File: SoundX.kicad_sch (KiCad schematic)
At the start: 51 parts, among them CN1 EDGE_CONN, CN2 AUDIO_OUT, CN3 CONN_MIDI_IN, CN4 CONN_MIDI_OUT, U1 GAL20V8, U2 MOS_6551_ACIA, U3 YM3526, U4 6N138, U6 YM3014, U7 LM324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

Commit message: Version with MC6850 should be ready
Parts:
- removed U2: MOS_6551_ACIA, Package_DIP:DIP-28_W15.24mm_Socket_LongPads, symbol W65C51S:W65C51S
- added U2: MC6850, Package_DIP:DIP-24_W15.24mm_Socket_LongPads, symbol Interface_UART:MC6850
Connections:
- net +5V: now also U2.10 (CS1), U2.12 (VCC), U2.8 (CS0)
- net GND: now also U2.1 (VSS), U2.23 (~{DCD}), U2.24 (~{CTS})
- net a0: now also U2.11 (RS)
- net clock_acia: now also U2.3 (Rx_CLK), U2.4 (Tx_CLK)
- net d0: now also U2.22 (D0)
- net d1: now also U2.21 (D1)
- net d2: now also U2.20 (D2)
- net d3: now also U2.19 (D3)
- net d4: now also U2.18 (D4)
- net d5: now also U2.17 (D5)
- net d6: now also U2.16 (D6)
- net d7: now also U2.15 (D7)
- net phi2: now also U2.14 (E)
- net r_~{w}: now also U2.13 (R/~{W})
- net rxd_ttl: now also U2.2 (Rx_Data)
- net txd_ttl: now also U2.6 (Tx_Data)
- net ~{irq}: now also U2.7 (~{IRQ})
- net ~{midi_cs}: now also U2.9 (CS2)
- net at FB3.2: now also R2.1; no longer R2.2
- net at X2.5 (OUT): now also R2.2; no longer R2.1
- no-connect marks 20 -> 18
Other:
- note added: "ACTIVE-LOW!"
- note removed: "NOTE 3 MHZ CRYSTAL! THIS ALLOWS REACHING THE 31250 BPS REQUIRED FOR MIDI CONFIGURING THE ACIA FOR 19200 BPS (DIVISOR = 96 => 3000000/96 = 31250) WE ALSO PROVIDE PARALLEL R AND SERIES C FOR W65C51S, BUT I'D RECOMMEND USING AN OLDER 6551"
- note removed: "Pin 7 must float with external clock"
- moved on the sheet: C11, R2

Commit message: Final touches for V2
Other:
- moved on the sheet: U1

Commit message: Fixes after rebasing (???)
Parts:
- JP1, JP2, JP3, JP4, JP5, JP6: now left out of the parts list
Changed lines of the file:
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@@
 		(unit 1)
 		(exclude_from_sim no)
-		(in_bom yes)
+		(in_bom no)
 		(on_board yes)
 		(dnp no)
@@
 		(unit 1)
 		(exclude_from_sim no)
-		(in_bom yes)
+		(in_bom no)
 		(on_board yes)
 		(dnp no)
@@
 		(unit 1)
 		(exclude_from_sim no)
-		(in_bom yes)
+		(in_bom no)
 		(on_board yes)
 		(dnp no)
@@
 		(unit 1)
 		(exclude_from_sim no)
-		(in_bom yes)
+		(in_bom no)
 		(on_board yes)
 		(dnp no)
@@
 		(unit 1)
 		(exclude_from_sim no)
-		(in_bom yes)
+		(in_bom no)
 		(on_board yes)
 		(dnp no)
@@
 		(unit 1)
 		(exclude_from_sim no)
-		(in_bom yes)
+		(in_bom no)
 		(on_board yes)
 		(dnp no)

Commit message: Readd some P/Ns and add 5mm-pitch footprint for DIN-5 connector
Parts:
- C1, C15: MouserPN (none) -> 710-860010472002
- C13: MouserPN 810-FG28C0G1H471JNT6 -> (none)
- C5: MouserPN 710-860020573008 -> 710-860010472002
- C7: MouserPN (none) -> 810-FG28X7R1H104KNT0
- CN1: now left out of the parts list
- FB1, FB2, FB3: MouserPN 623-2743015112 -> 875-28C0236-0EW-10
- JP1, JP2, JP3, JP4, JP5, JP6: MouserPN (none) -> -
- U1: MouserPN (none) -> 556-AF22LV10CQZ-30PU
- U2, X2: Notes (none) -> MIDI
- U4: MouserPN (none) -> 859-6N138
- U7: MouserPN (none) -> 595-LM324N
- X1: MouserPN (none) -> 520-TCH357-X; Notes (none) -> OPL
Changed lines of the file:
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@@
 			)
 		)
+		(property "MouserPN" "-"
+			(at 351.409 142.113 0)
+			(effects
+				(font
+					(size 1.27 1.27)
+				)
+				(hide yes)
+			)
+		)
 		(pin "1"
 		)
@@
 			)
 		)
+		(property "MouserPN" "-"
+			(at 322.326 230.632 0)
+			(effects
+				(font
+					(size 1.27 1.27)
+				)
+				(hide yes)
+			)
+		)
 		(pin "1"
 		)
@@
 			)
 		)
+		(property "MouserPN" "-"
+			(at 340.487 221.869 0)
+			(effects
+				(font
+					(size 1.27 1.27)
+				)
+				(hide yes)
+			)
+		)
 		(pin "1"
 		)
@@
 			)
 		)
+		(property "MouserPN" "859-6N138"
+			(at 212.725 228.727 0)
+			(effects
+				(font
+					(size 1.27 1.27)
+				)
+				(hide yes)
+			)
+		)
 		(pin "1"
 		)
@@
 		(unit 1)
 		(exclude_from_sim no)
-		(in_bom yes)
+		(in_bom no)
 		(on_board yes)
 		(dnp no)
@@
 			)
 		)
-		(property "Datasheet" "DOCUMENTATION"
+		(property "Datasheet" ""
 			(at 60.96 104.14 0)
 			(effects
@@
 			)
 		)
+		(property "MouserPN" "556-AF22LV10CQZ-30PU"
+			(at 346.71 66.04 0)
+			(effects
+				(font
+					(size 1.27 1.27)
+				)
+				(hide yes)
+			)
+		)
 		(pin "12"
 		)
@@
 			)
 		)
-		(property "MouserPN" "810-FG28C0G1H471JNT6"
+		(property "MouserPN" ""
 			(at 252.603 166.751 0)
 			(effects
@@
 			)
 		)
+		(property "MouserPN" "810-FG28X7R1H104KNT0"
+			(at 38.1 175.26 0)
+			(effects
+				(font
+					(size 1.27 1.27)
+				)
+				(hide yes)
+			)
+		)
 		(pin "1"
 		)
@@
 			)
 		)
-		(property "MouserPN" "623-2743015112"
+		(property "MouserPN" "875-28C0236-0EW-10"
 			(at 123.952 199.39 0)
 			(effects
@@
 			)
 		)
+		(property "MouserPN" "-"
+			(at 59.69 175.26 0)
+			(effects
+				(font
+					(size 1.27 1.27)
+				)
+				(hide yes)
+			)
+		)
 		(pin "1"
 		)
@@
 			)
 		)
-		(property "MouserPN" "623-2743015112"
+		(property "MouserPN" "875-28C0236-0EW-10"
 			(at 29.21 26.543 0)
 			(effects
@@
 			)
 		)
+		(property "MouserPN" "710-860010472002"
+			(at 101.981 263.398 0)
+			(effects
+				(font
+					(size 1.27 1.27)
+				)
+				(hide yes)
+			)
+		)
 		(pin "1"
 		)
@@
 			)
 		)
+		(property "MouserPN" "-"
+			(at 300.355 151.13 0)
+			(effects
+				(font
+					(size 1.27 1.27)
+				)
+				(hide yes)
+			)
+		)
 		(pin "1"
 		)
@@
 			)
 		)
+		(property "MouserPN" "595-LM324N"
+			(at 229.489 159.258 0)
+			(effects
+				(font
+					(size 1.27 1.27)
+				)
+				(hide yes)
+			)
+		)
 		(pin "1"
 		)
@@
 			)
 		)
+		(property "MouserPN" "595-LM324N"
+			(at 319.659 137.033 0)
+			(effects
+				(font
+					(size 1.27 1.27)
+				)
+				(hide yes)
+			)
+		)
 		(pin "1"
 		)
@@
 			)
 		)
+		(property "MouserPN" "595-LM324N"
+			(at 276.86 161.798 0)
+			(effects
+				(font
+					(size 1.27 1.27)
+				)
+				(hide yes)
+			)
+		)
 		(pin "1"
 		)
@@
 			)
 		)
+		(property "MouserPN" "595-LM324N"
+			(at 281.94 134.493 0)
+			(effects
+				(font
+					(size 1.27 1.27)
+				)
+				(hide yes)
+			)
+		)
 		(pin "1"
 		)
@@
 			)
 		)
+		(property "MouserPN" "595-LM324N"
+			(at 91.186 263.017 0)
+			(effects
+				(font
+					(size 1.27 1.27)
+				)
+				(hide yes)
+			)
+		)
 		(pin "1"
 		)
@@
 			)
 		)
-		(property "MouserPN" "710-860020573008"
+		(property "MouserPN" "710-860010472002"
 			(at 266.954 138.303 0)
 			(effects
@@
 			)
 		)
+		(property "MouserPN" "710-860010472002"
+			(at 341.249 137.033 0)
+			(effects
+				(font
+					(size 1.27 1.27)
+				)
+				(hide yes)
+			)
+		)
 		(pin "1"
 		)
@@
 			)
 		)
-		(property "MouserPN" "623-2743015112"
+		(property "MouserPN" "875-28C0236-0EW-10"
 			(at 123.952 175.26 0)
 			(effects
@@
 			)
 		)
+		(property "Notes" "MIDI"
+			(at 97.79 175.26 0)
+			(effects
+				(font
+					(size 1.27 1.27)
+				)
+				(hide yes)
+			)
+		)
 		(pin "1"
 		)
@@
 			)
 		)
+		(property "MouserPN" "-"
+			(at 85.09 175.26 0)
+			(effects
+				(font
+					(size 1.27 1.27)
+				)
+				(hide yes)
+			)
+		)
 		(pin "1"
 		)
@@
 			)
 		)
+		(property "Notes" "MIDI"
+			(at 228.6 64.77 0)
+			(effects
+				(font
+					(size 1.27 1.27)
+				)
+				(hide yes)
+			)
+		)
 		(pin "10"
 		)
@@
 			(at 72.39 175.26 0)
 			(effects
+				(font
+					(size 1.27 1.27)
+				)
+				(hide yes)
+			)
+		)
+		(property "MouserPN" "520-TCH357-X"
+			(at 72.39 175.26 0)
+			(effects
+				(font
+					(size 1.27 1.27)
+				)
+				(hide yes)
+			)
+		)
+		(property "Notes" "OPL"
+			(at 72.39 175.26 0)
+			(effects

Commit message: Add clock divider for ACIA
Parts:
- added C12: 100n, Capacitor_THT:C_Disc_D7.0mm_W2.5mm_P5.00mm, symbol Device:C
- added JP7: JMP_ACIA_CLK, Jumper:SolderJumper-3_P1.3mm_Open_RoundedPad1.0x1.5mm, symbol Jumper:Jumper_3_Open
- added U5: 74HCT74, Package_DIP:DIP-14_W7.62mm_Socket_LongPads, symbol 74xx:74LS74
- V0, V1: now left out of the parts list
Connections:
- net +5V: now also C12.1, U5.1 (~{R}), U5.10 (~{S}), U5.13 (~{R}), U5.14 (VCC), U5.4 (~{S})
- net GND: now also C12.2, U5.7 (GND)
- net clock_acia: now also JP7.2 (C); no longer FB3.1
- new net: U5.2 (D), U5.6 (~{Q})
- new net: U5.12 (D), U5.8 (~{Q})
- new net clk: FB3.1, JP7.1 (A), U5.3 (C)
- new net clk_half: U5.11 (C), U5.5 (Q)
- new net clk_quarter: JP7.3 (B), U5.9 (Q)
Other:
- note added: "ACIA CLOCK GENERATOR"
- note added: "OR GAL22V10"
- note added: "RATIONALE: Unfortunately I can't remember why, but some time ago I had realized that, while the MC6850 would be able to reach the MIDI baud rate (31250 bps) with either a 500 kHz or a 2 MHz crystal, the former option was better. Probably it was for backwards compatibility with something but I cannot recall what. Anyway, it seems that 500 kHz oscillators are difficult to come by, so I added a doub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"
- note added: "YM CIRCUIT"
- note removed: "CLOCK GENERATOR"
- note removed: "OR GAL22V16"
- moved on the sheet: C1, C11, C13, C4, C5, C6, C7, CN2, CN3, CN4, D1, FB2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

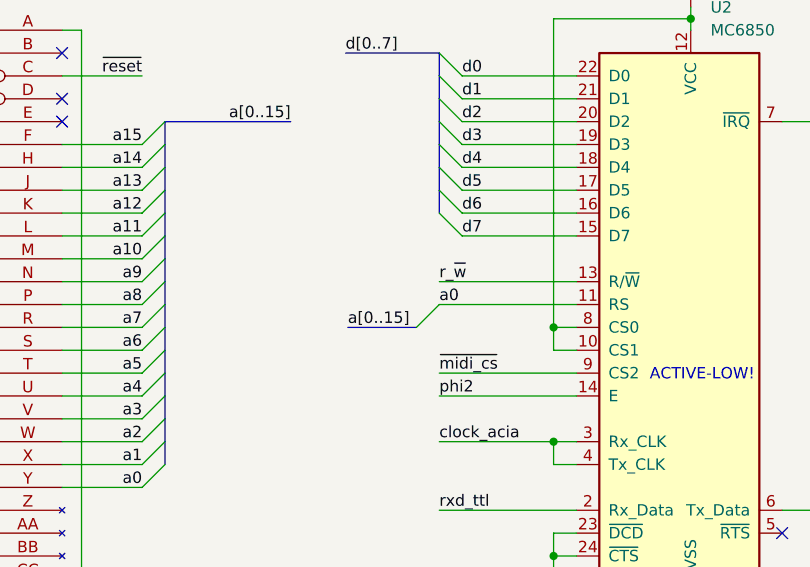
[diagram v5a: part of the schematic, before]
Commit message: Add RW/A1 jumper This is inspired by some C64 interfaces
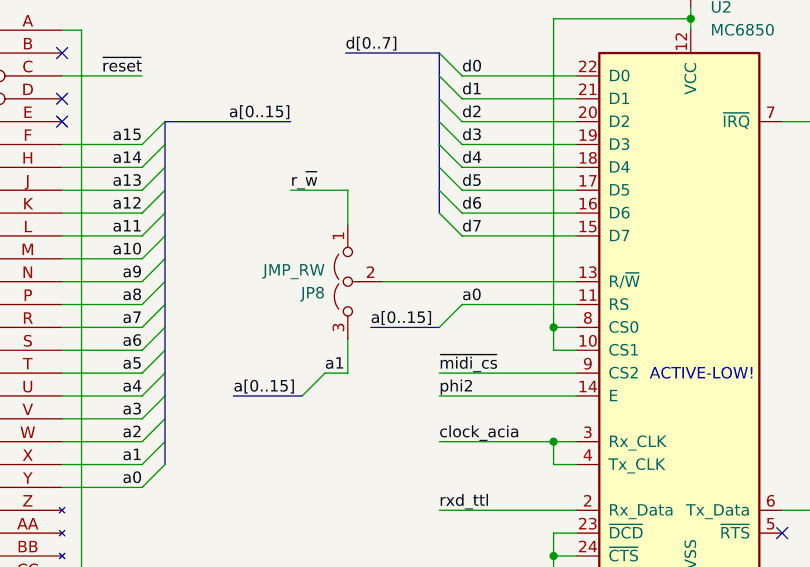
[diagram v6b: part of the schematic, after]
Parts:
- added JP8: JMP_RW, Jumper:SolderJumper-3_P1.3mm_Open_RoundedPad1.0x1.5mm, symbol SoundX-rescue:Jumper_3_Open-Jumper
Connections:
- net a1: now also JP8.3 (B)
- net r_~{w}: now also JP8.1 (A); no longer U2.13 (R/~{W})
- new net: JP8.2 (C), U2.13 (R/~{W})
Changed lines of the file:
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@@
 	)
 	(bus_entry
-		(at 119.38 62.23)
+		(at 121.92 62.23)
 		(size 2.54 -2.54)
 		(stroke
@@
 	)
 	(bus_entry
+		(at 106.68 69.85)
+		(size 2.54 -2.54)
+		(stroke
+			(width 0)
+			(type default)
+		)
+	)
+	(bus_entry
 		(at 191.77 54.61)
 		(size 2.54 2.54)
@@
 		)
 	)
+	(bus
+		(pts
+			(xy 99.06 69.85) (xy 106.68 69.85)
+		)
+		(stroke
+			(width 0)
+			(type default)
+		)
+	)
 	(wire
 		(pts
@@
 	(wire
 		(pts
+			(xy 111.76 63.5) (xy 111.76 67.31)
+		)
+		(stroke
+			(width 0)
+			(type default)
+		)
+	)
+	(wire
+		(pts
 			(xy 289.56 143.51) (xy 289.56 138.43)
 		)
@@
 	(wire
 		(pts
+			(xy 109.22 67.31) (xy 111.76 67.31)
+		)
+		(stroke
+			(width 0)
+			(type default)
+		)
+	)
+	(wire
+		(pts
 			(xy 29.21 34.29) (xy 29.21 31.75)
 		)
@@
 	(wire
 		(pts
-			(xy 137.16 59.69) (xy 121.92 59.69)
+			(xy 137.16 59.69) (xy 124.46 59.69)
 		)
 		(stroke
@@
 	(bus
 		(pts
-			(xy 111.76 62.23) (xy 119.38 62.23)
+			(xy 114.3 62.23) (xy 121.92 62.23)
 		)
 		(stroke
@@
 	(wire
 		(pts
+			(xy 115.57 57.15) (xy 137.16 57.15)
+		)
+		(stroke
+			(width 0)
+			(type default)
+		)
+	)
+	(wire
+		(pts
 			(xy 229.87 207.01) (xy 229.87 198.12)
 		)
@@
 	(wire
 		(pts
-			(xy 121.92 57.15) (xy 137.16 57.15)
+			(xy 41.91 34.29) (xy 29.21 34.29)
 		)
 		(stroke
@@
 		)
 	)
-	(wire
+	(bus
 		(pts
-			(xy 41.91 34.29) (xy 29.21 34.29)
+			(xy 144.526 168.91) (xy 82.55 168.91)
 		)
 		(stroke
@@
 	(bus
 		(pts
-			(xy 144.526 168.91) (xy 82.55 168.91)
+			(xy 144.526 161.29) (xy 144.526 168.91)
 		)
 		(stroke
@@
 		)
 	)
-	(bus
+	(wire
 		(pts
-			(xy 144.526 161.29) (xy 144.526 168.91)
+			(xy 121.92 217.17) (xy 121.92 219.71)
 		)
 		(stroke
@@
 	(wire
 		(pts
-			(xy 121.92 217.17) (xy 121.92 219.71)
+			(xy 111.76 50.8) (xy 111.76 46.99)
 		)
 		(stroke
@@
 	(wire
 		(pts
+			(xy 105.41 46.99) (xy 111.76 46.99)
+		)
+		(stroke
+			(width 0)
+			(type default)
+		)
+	)
+	(wire
+		(pts
 			(xy 41.91 64.77) (xy 29.21 64.77)
 		)
@@
 		)
 	)
+	(label "a1"
+		(at 109.22 67.31 0)
+		(fields_autoplaced yes)
+		(effects
+			(font
+				(size 1.27 1.27)
+			)
+			(justify left bottom)
+		)
+	)
 	(label "d0"
 		(at 85.09 153.67 0)
@@
 	)
 	(label "r_~{w}"
-		(at 121.92 57.15 0)
+		(at 105.41 46.99 0)
 		(fields_autoplaced yes)
 		(effects
@@
 		)
 	)
+	(label "a[0..15]"
+		(at 99.06 69.85 0)
+		(fields_autoplaced yes)
+		(effects
+			(font
+				(size 1.27 1.27)
+			)
+			(justify left bottom)
+		)
+	)
 	(label "a0"
-		(at 121.92 59.69 0)
+		(at 124.46 59.69 0)
 		(fields_autoplaced yes)
 		(effects
@@
 	)
 	(label "a[0..15]"
-		(at 111.76 62.23 0)
+		(at 114.3 62.23 0)
 		(fields_autoplaced yes)
 		(effects
@@
 					(unit 1)
 				)
+			)
+		)
+	)
+	(symbol
+		(lib_id "SoundX-rescue:Jumper_3_Open-Jumper")
+		(at 111.76 57.15 90)
+		(mirror x)
+		(unit 1)
+		(exclude_from_sim no)
+		(in_bom no)
+		(on_board yes)
+		(dnp no)
+		(property "Reference" "JP8"
+			(at 109.22 58.4201 90)
+			(effects
+				(font
+					(size 1.27 1.27)
+				)
+				(justify left)
+			)
+		)
+		(property "Value" "JMP_RW"
+			(at 109.22 55.8801 90)
+			(effects
+				(font
+					(size 1.27 1.27)
+				)
+				(justify left)
+			)
+		)
+		(property "Footprint" "Jumper:SolderJumper-3_P1.3mm_Open_RoundedPad1.0x1.5mm"
+			(at 111.76 57.15 0)
+			(effects
+				(font
+					(size 1.27 1.27)
+				)
+				(hide yes)
+			)
+		)
+		(property "Datasheet" "~"
+			(at 111.76 57.15 0)
+			(effects
+				(font
+					(size 1.27 1.27)
+				)
+				(hide yes)
+			)
+		)
+		(property "Description" ""
+			(at 111.76 57.15 0)
+			(effects
+				(font
+					(size 1.27 1.27)
+				)
+				(hide yes)
+			)
+		)
+		(property "Notes" "OPL"
+			(at 111.76 57.15 0)
+			(effects
+				(font
+					(size 1.27 1.27)
+				)
+				(hide yes)
+			)
+		)
+		(property "MouserPN" "-"
+			(at 111.76 57.15 0)
+			(effects
+				(font
+					(size 1.27 1.27)
+				)
+				(hide yes)
+			)
+		)
+		(pin "1"
+		)
+		(pin "2"
+		)
+		(pin "3"
+		)
+		(instances
+			(project "SoundX"
+				(path "/03a251b6-65fe-465c-8232-d6f8713652f2"
+					(reference "JP8")
+					(unit 1)
+				)

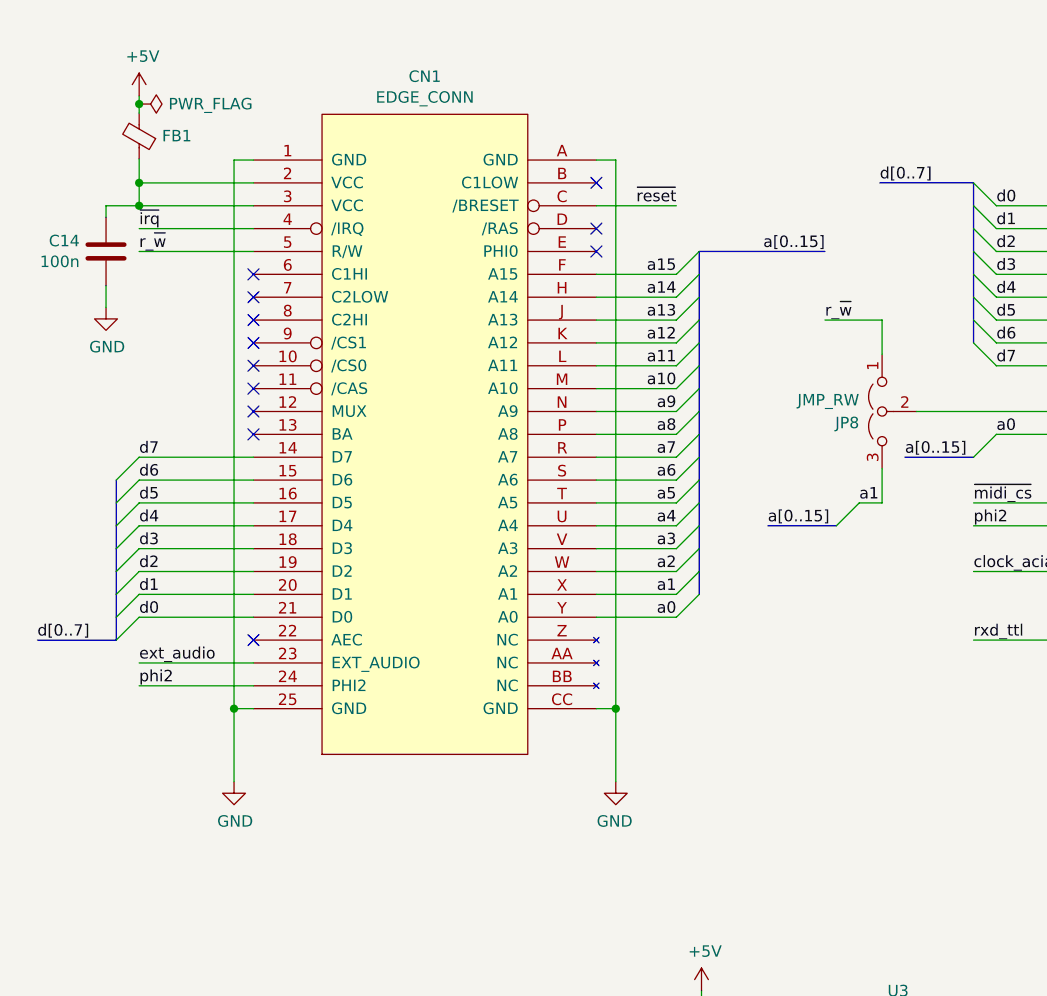
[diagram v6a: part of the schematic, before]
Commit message: 44-pin version of V2
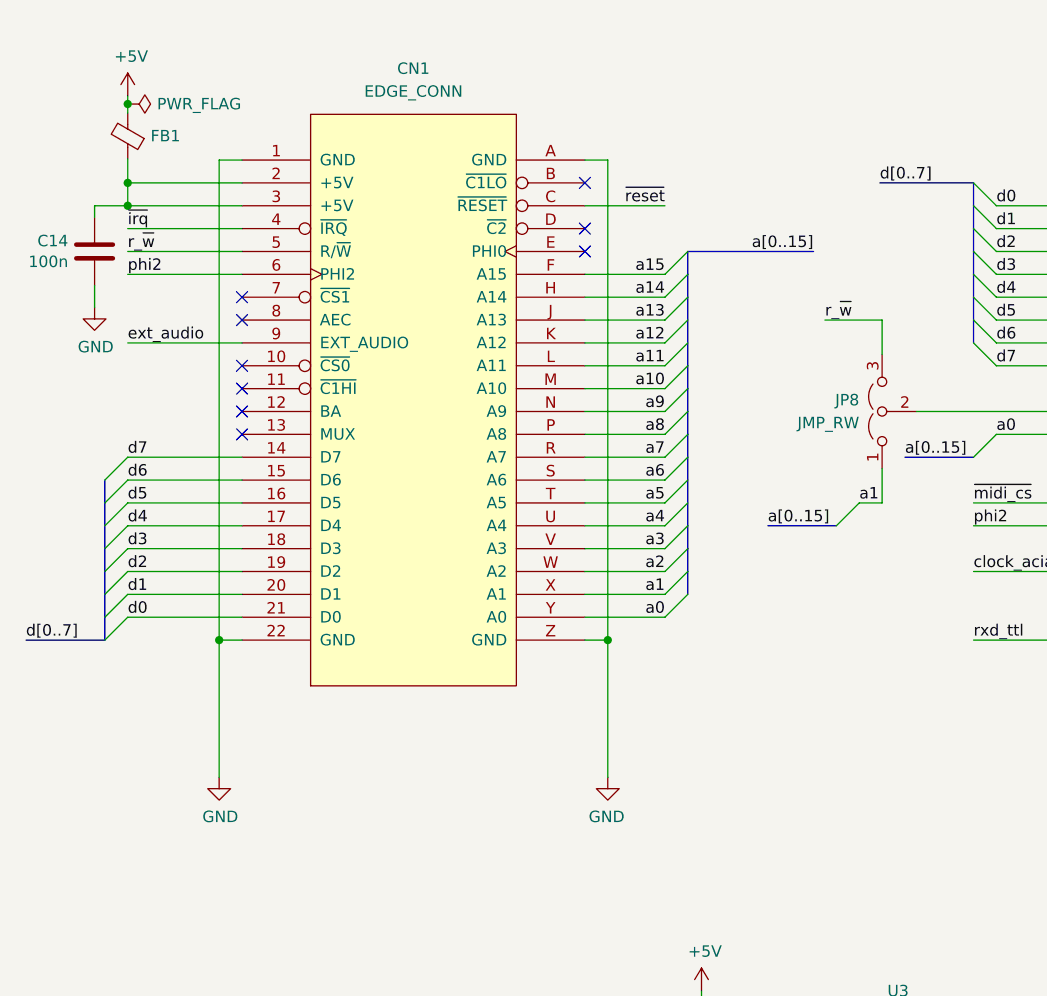
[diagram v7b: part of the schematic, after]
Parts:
- removed CN1: EDGE_CONN, SoundX:C16_Cart_Conn, symbol C16-Exp-Port:C16-Exp-Port
- added CN1: EDGE_CONN, SoundX:EdgeConn-44pin, symbol C16-Exp-Port-44pin-In:C16_NEWSTYLE_EXP_PORT
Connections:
- net GND: now also CN1.1 (GND), CN1.22 (GND), CN1.A (GND), CN1.Z (GND)
- net a0: now also CN1.Y (A0)
- net a1: now also JP8.1 (A), CN1.X (A1); no longer JP8.3 (B)
- net a10: now also CN1.M (A10)
- net a11: now also CN1.L (A11)
- net a12: now also CN1.K (A12)
- net a13: now also CN1.J (A13)
- net a14: now also CN1.H (A14)
- net a15: now also CN1.F (A15)
- net a2: now also CN1.W (A2)
- net a3: now also CN1.V (A3)
- net a4: now also CN1.U (A4)
- net a5: now also CN1.T (A5)
- net a6: now also CN1.S (A6)
- net a7: now also CN1.R (A7)
- net a8: now also CN1.P (A8)
- net a9: now also CN1.N (A9)
- net d0: now also CN1.21 (D0)
- net d1: now also CN1.20 (D1)
- net d2: now also CN1.19 (D2)
- net d3: now also CN1.18 (D3)
- net d4: now also CN1.17 (D4)
- net d5: now also CN1.16 (D5)
- net d6: now also CN1.15 (D6)
- net d7: now also CN1.14 (D7)
- net ext_audio: now also CN1.9 (EXT_AUDIO)
- net phi2: now also CN1.6 (PHI2)
- net r_~{w}: now also JP8.3 (B), CN1.5 (R/~{W}); no longer JP8.1 (A)
- net ~{irq}: now also CN1.4 (~{IRQ})
- net ~{reset}: now also CN1.C (~{RESET})
- net at C14.1, FB1.1: now also CN1.2 (+5V), CN1.3 (+5V)
- no-connect marks 18 -> 15
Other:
- moved on the sheet: C14, FB1
